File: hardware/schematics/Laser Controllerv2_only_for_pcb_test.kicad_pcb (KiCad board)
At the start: 2 copper layers, 175 x 115 mm, 116 parts, among them J1 SD Card Module (6-pin, 2.54mm), J2 12.6V IN (BUCK), J3 PWR IN Galvo, J4 FAN1 12V IN, J5 FAN1, J6 FAN2 12V IN, J7 FAN2, U1 ESP32-S3-N16R8-DevKit, U10 DS18B20 connector, U12 OPA4134UA_2K5, U13 Galvo Input, U15 6N137, U16 6N137, U17 6N137, U2 DAC8562SDGST, U3 TTL_RGB Blue, U4 TTL_RGB Red, U5 TTL_RGB Green, U6 DS18B20 connector, U7 DS18B20 connector, U8 DS18B20 connector, U9 DS18B20 connector

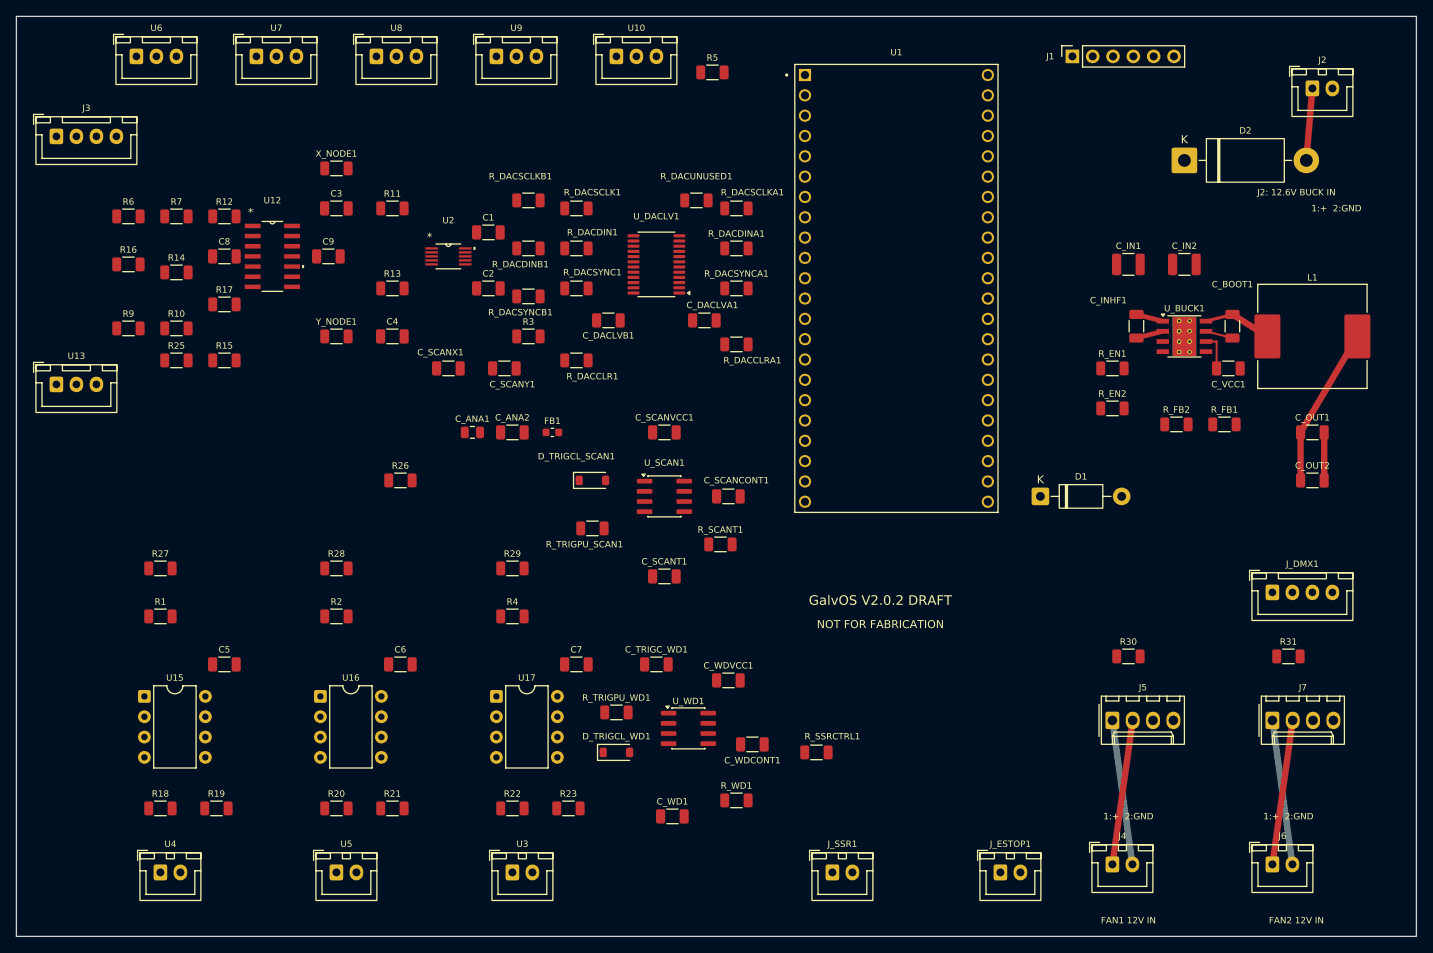
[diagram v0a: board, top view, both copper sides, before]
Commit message: feat(hw): route v2.0.3 draft and add ground planes
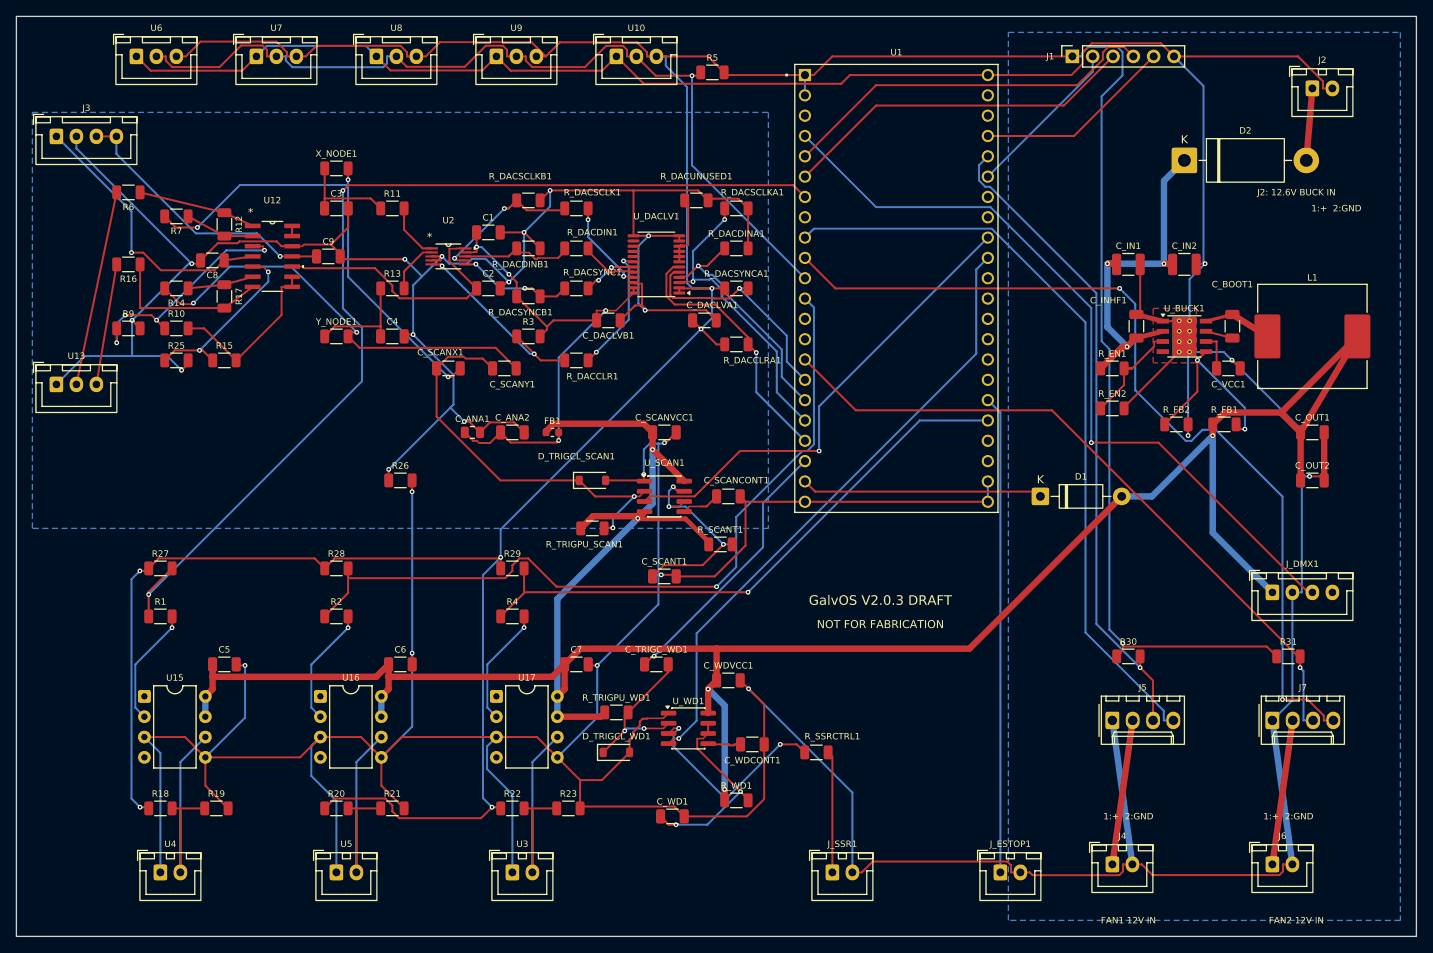
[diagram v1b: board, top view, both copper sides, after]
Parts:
- moved R6 3.00 mm to (14.0, 22.0), turned to 180 degrees
- moved R14 2.00 mm to (20.0, 34.0), turned to 180 degrees
- moved C8 1.58 mm to (24.5, 30.5), turned to 180 degrees
- moved R12 1.00 mm to (26.0, 26.0), turned to -90 degrees
- moved R17 1.00 mm to (26.0, 35.0), turned to -90 degrees
- turned R16 to 180 degrees
- turned R7 to 180 degrees
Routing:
- net 5V GND Buck: track 45.8 -> 788.3 mm, vias 0 -> 12
- net +3V3: track 0.00 -> 456.2 mm, vias 0 -> 7
- net Buck +5V: track 19.9 -> 335.8 mm, vias 0 -> 5
- net AGND (from Galvo Board): track 0.00 -> 249.0 mm, vias 0 -> 13
- net /GPIO7: track 0.00 -> 128.7 mm, vias 0 -> 2
- net /FAN2_PWM: track 0.00 -> 112.7 mm, vias 0 -> 2
- net Net-(U1-GPIO18): track 0.00 -> 111.0 mm, vias 0 -> 1
- net /GPIO8: track 0.00 -> 98.0 mm, vias 0 -> 1
- net /GPIO4: track 0.00 -> 96.9 mm, vias 0 -> 1
- net /FAN1_PWM: track 0.00 -> 95.4 mm
- net /FAN2_TACH: track 0.00 -> 86.6 mm, vias 0 -> 1
- net /FAN1_TACH: track 0.00 -> 81.7 mm, vias 0 -> 1
- net /GPIO38: track 0.00 -> 77.6 mm, vias 0 -> 1
- net /GPIO21: track 0.00 -> 74.1 mm, vias 0 -> 1
- net /+5V_ANA: track 0.00 -> 66.5 mm, vias 0 -> 4
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- added copper zone on B.Cu, net 5V GND Buck
- added copper zone on F.Cu, net 5V GND Buck
- added copper zone on B.Cu, net AGND (from Galvo Board)
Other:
- board text added: "GalvOS V2.0.3 DRAFT"
- board text removed: "GalvOS V2.0.2 DRAFT"

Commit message: fix(hw): buffer scan-status GPIO in v2.0.4
Remove direct 5 V timer drive of GPIO39 while preserving polarity.
Keep the draft unreleased pending safety and physical validation.
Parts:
- added C_SCANLV1: 100nF, Capacitor_SMD:C_1206_3216Metric, F.Cu at (125.5, 31.5)
- added R_SCANIN1: 10k, Resistor_SMD:R_1206_3216Metric, F.Cu at (133.0, 29.0)
- added U_SCANLV1: SN74LVC1G17DBVR, Package_TO_SOT_SMD:SOT-23-5, F.Cu at (128.0, 27.6)
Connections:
- U_SCAN1 pad 3: /GPIO39 -> /SCAN_STATUS_5V
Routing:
- net /SCAN_STATUS_5V: track 0.00 -> 72.8 mm, vias 0 -> 2
- net /GPIO39: track 59.8 -> 5.83 mm, vias 1 -> 0
- net 5V GND Buck: track 788.3 -> 803.7 mm, vias 12 -> 14
- net +3V3: track 456.2 -> 470.9 mm, vias 7 -> 8
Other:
- board text added: "GalvOS V2.0.4 DRAFT"
- board text removed: "GalvOS V2.0.3 DRAFT"

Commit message: fix(hw): protect DMX GPIO in v2.0.5
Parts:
- added C_DMXLV1: 100nF, Capacitor_SMD:C_1206_3216Metric, F.Cu at (125.5, 20.9)
- added R_DMXIN1: 10k, Resistor_SMD:R_1206_3216Metric, F.Cu at (133.0, 18.5)
- added U_DMXLV1: SN74LVC1G17DBVR, Package_TO_SOT_SMD:SOT-23-5, F.Cu at (128.0, 17.0)
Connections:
- J_DMX1 pad 3: /GPIO4 -> /DMX_RO_5V
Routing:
- net /DMX_RO_5V: track 0.00 -> 86.1 mm, vias 0 -> 2
- net /GPIO4: track 96.9 -> 39.0 mm
- net 5V GND Buck: track 803.7 -> 834.0 mm, vias 14 -> 15
- net +3V3: track 470.9 -> 482.8 mm, vias 8 -> 9
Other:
- board text added: "GalvOS V2.0.5 DRAFT"
- board text removed: "GalvOS V2.0.4 DRAFT"

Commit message: fix(hw): shorten buck feedback in v2.0.6
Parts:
- C_INHF1: value 100nF -> 220nF
- moved R_FB2 6.50 mm to (145.2, 44.5), turned to 180 degrees
- moved R_FB1 3.61 mm to (149.0, 48.0), turned to 90 degrees
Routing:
- net /FB_BUCK: track 23.7 -> 6.55 mm, vias 2 -> 0
- net 5V GND Buck: track 834.0 -> 825.4 mm, vias 15 -> 14
- net Buck +5V: track 335.8 -> 337.8 mm
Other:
- board text added: "GalvOS V2.0.6 DRAFT"
- board text removed: "GalvOS V2.0.5 DRAFT"

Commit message: fix(hw): localize buck input loop in v2.0.7
Preserve circuit values while shortening local capacitor paths.
Remove two exact duplicate copper objects and guard ID uniqueness.
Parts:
- moved C_IN2 12.2 mm to (136.5, 38.7), turned to 90 degrees
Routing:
- net +3V3: track 482.8 -> 480.0 mm
- net /VIN_BUCK: track 44.2 -> 46.6 mm, vias 3 -> 2
- net 5V GND Buck: track 825.4 -> 827.8 mm, vias 14 -> 13
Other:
- board text added: "GalvOS V2.0.7 DRAFT"
- board text removed: "GalvOS V2.0.6 DRAFT"
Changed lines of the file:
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@@
 		(title "GalvOS Laser Controller V2")
 		(date "2026-09-14")
-		(rev "V2.0.6 DRAFT")
+		(rev "V2.0.7 DRAFT")
 		(comment 1 "NOT FOR FABRICATION OR LASER OPERATION")
 	)
@@
 	(footprint "Capacitor_SMD:C_1210_3225Metric"
 		(layer "F.Cu")
-		(at 146 31)
+		(at 136.5 38.73 90)
 		(descr "Capacitor SMD 1210 (3225 Metric), square (rectangular) end terminal, IPC-7351 nominal, (Body size source: IPC-SM-782 page 76, https://www.pcb-3d.com/wordpress/wp-content/uploads/ipc-sm-782a_amendment_1_and_2.pdf)")
 		(tags "capacitor")
 		(property "Reference" "C_IN2"
-			(at 0 -2.3 0)
+			(at 4.03 0 0)
 			(layer "F.SilkS")
 			(effects
@@
 		)
 		(property "Value" "10uF"
-			(at 0 2.3 0)
+			(at 0 2.3 90)
 			(layer "F.Fab")
 			(effects
@@
 		)
 		(property "Datasheet" ""
-			(at 0 0 0)
+			(at 0 0 90)
 			(layer "F.Fab")
 			(hide yes)
@@
 		)
 		(property "Description" "Unpolarized capacitor"
-			(at 0 0 0)
+			(at 0 0 90)
 			(layer "F.Fab")
 			(hide yes)
@@
 		)
 		(property "KiLib_Generator" "SMD_2terminal_chip_molded"
-			(at 0 0 0)
+			(at 0 0 90)
 			(layer "F.SilkS")
 			(hide yes)
@@
 		)
 		(fp_text user "${REFERENCE}"
-			(at 0 0 0)
+			(at 0 0 90)
 			(layer "F.Fab")
 			(effects
@@
 		)
 		(pad "1" smd roundrect
-			(at -1.475 0)
+			(at -1.475 0 90)
 			(size 1.15 2.7)
 			(layers "F.Cu" "F.Mask" "F.Paste")
@@
 		)
 		(pad "2" smd roundrect
-			(at 1.475 0)
+			(at 1.475 0 90)
 			(size 1.15 2.7)
 			(layers "F.Cu" "F.Mask" "F.Paste")
@@
 				(font
 					(size 1.27 1.27)
+					(thickness 0.15)
 				)
 			)
@@
 				(font
 					(size 1.27 1.27)
+					(thickness 0.15)
 				)
 			)
@@
 				(font
 					(size 1.27 1.27)
+					(thickness 0.15)
 				)
 			)
@@
 		(tags "capacitor")
 		(property "Reference" "C_INHF1"
-			(at 3.23 -3.5 0)
+			(at 4.23 2.5 0)
 			(layer "F.SilkS")
 			(effects
@@
 				(font
 					(size 1.27 1.27)
+					(thickness 0.15)
 				)
 			)
@@
 				(font
 					(size 1.27 1.27)
+					(thickness 0.15)
 				)
 			)
@@
 				(font
 					(size 1.27 1.27)
+					(thickness 0.15)
 				)
 			)
@@
 		)
 	)
-	(gr_text "GalvOS V2.0.6 DRAFT"
+	(gr_text "GalvOS V2.0.7 DRAFT"
 		(at 108 73 0)
 		(layer "F.SilkS")
@@
 	)
 	(segment
-		(start 85.5913 39.0662)
-		(end 87.5251 41)
-		(width 0.25)
-		(layer "F.Cu")
-		(net "+3V3")
-	)
-	(segment
 		(start 47.8658 100.227)
 		(end 58.087 100.227)
@@
 	)
 	(segment
-		(start 85.5912 39.0662)
-		(end 85.5913 39.0662)
-		(width 0.25)
-		(layer "F.Cu")
-		(net "+3V3")
-	)
-	(segment
 		(start 33.8233 5)
 		(end 33.8233 4.4852)
@@
 	)
 	(segment
-		(start 144.439 30.9138)
-		(end 144.525 31)
-		(width 0.8)
+		(start 135.5375 44)
+		(end 135.538 44)
+		(width 0.25)
 		(layer "F.Cu")
 		(net "/VIN_BUCK")
 	)
 	(segment
-		(start 135.5375 44)
-		(end 135.538 44)
-		(width 0.25)
+		(start 136.5 40.205)
+		(end 140 40.205)
+		(width 0.8)
 		(layer "F.Cu")
 		(net "/VIN_BUCK")
@@
 	)
 	(segment
-		(start 143.447 30.9138)
-		(end 144.439 30.9138)
-		(width 0.8)
-		(layer "F.Cu")
-		(net "/VIN_BUCK")
-	)
-	(segment
 		(start 137.439 30.9138)
 		(end 137.525 31)
@@
 	)
 	(via
-		(at 143.447 30.9138)
-		(size 0.6)
-		(drill 0.3)
-		(layers "F.Cu" "B.Cu")
-		(net "/VIN_BUCK")
-	)
-	(via
 		(at 136.377 30.9138)
 		(size 0.6)
@@
 	)
 	(segment
-		(start 147.561 30.9138)
-		(end 147.475 31)
-		(width 0.25)
-		(layer "F.Cu")
-		(net "5V GND Buck")
-	)
-	(segment
 		(start 23.62 92.62)
 		(end 23.62 96.1575)
@@
 	)
 	(segment
+		(start 136.5 37.255)
+		(end 140 37.255)
+		(width 0.8)
+		(layer "F.Cu")
+		(net "5V GND Buck")
+	)
+	(segment
 		(start 129.138 26.7)
 		(end 129.138 25.8765)
@@
 	)
 	(segment
-		(start 148.59 30.9138)
-		(end 147.561 30.9138)
-		(width 0.25)
-		(layer "F.Cu")
-		(net "5V GND Buck")
-	)
-	(segment
 		(start 46.7569 6.7569)
 		(end 45 5)
@@
 		(size 0.6)
 		(drill 0.3)
-		(layers "F.Cu" "B.Cu")
-		(net "5V GND Buck")
-	)
-	(via
-		(at 148.59 30.9138)
-		(size 0.6)
-		(drill 0.3)

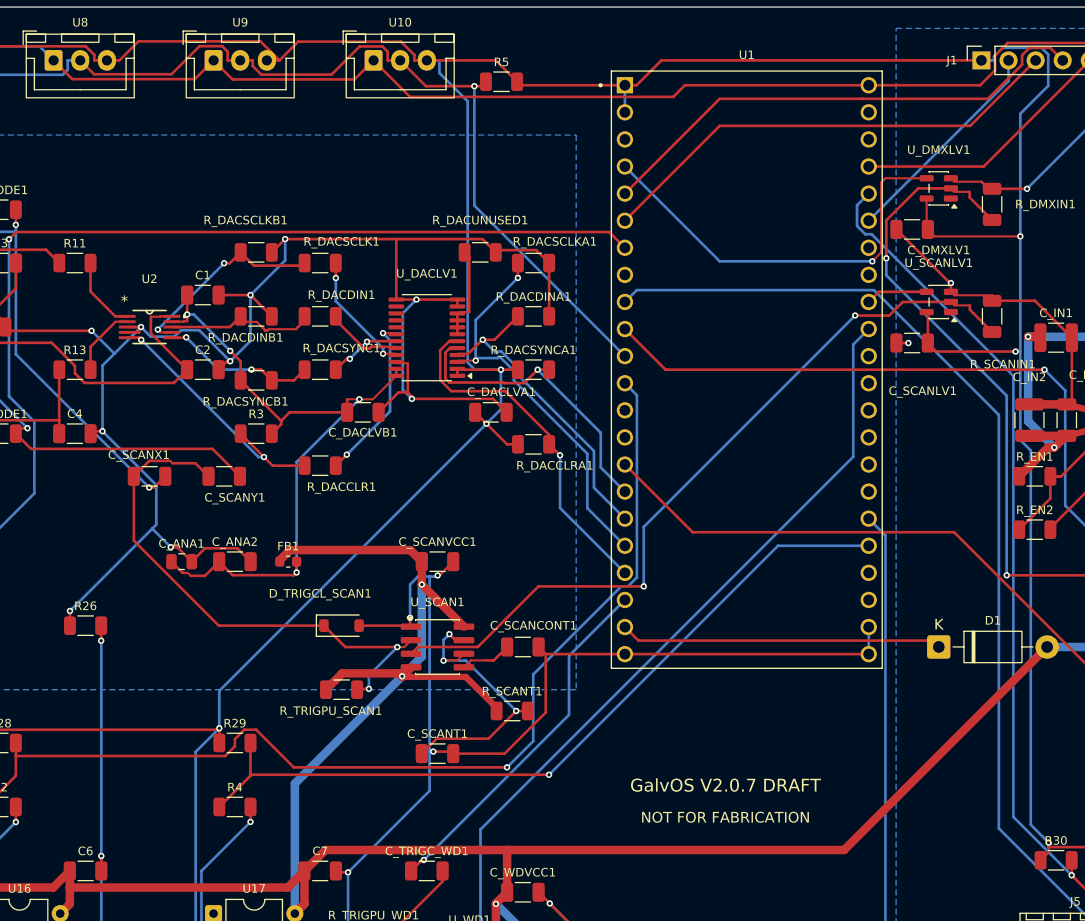
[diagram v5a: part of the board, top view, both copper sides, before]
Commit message: fix(hw): refine return copper and clearance in v2.0.8
Use the reported 28x57 mm module envelope without moving socket pads.
Clear bypass-capacitor collisions and improve local DAC return copper.

Keep the board a draft: row spacing, shutdown, load and physical
qualification remain open. Firmware and KiBot are unchanged.
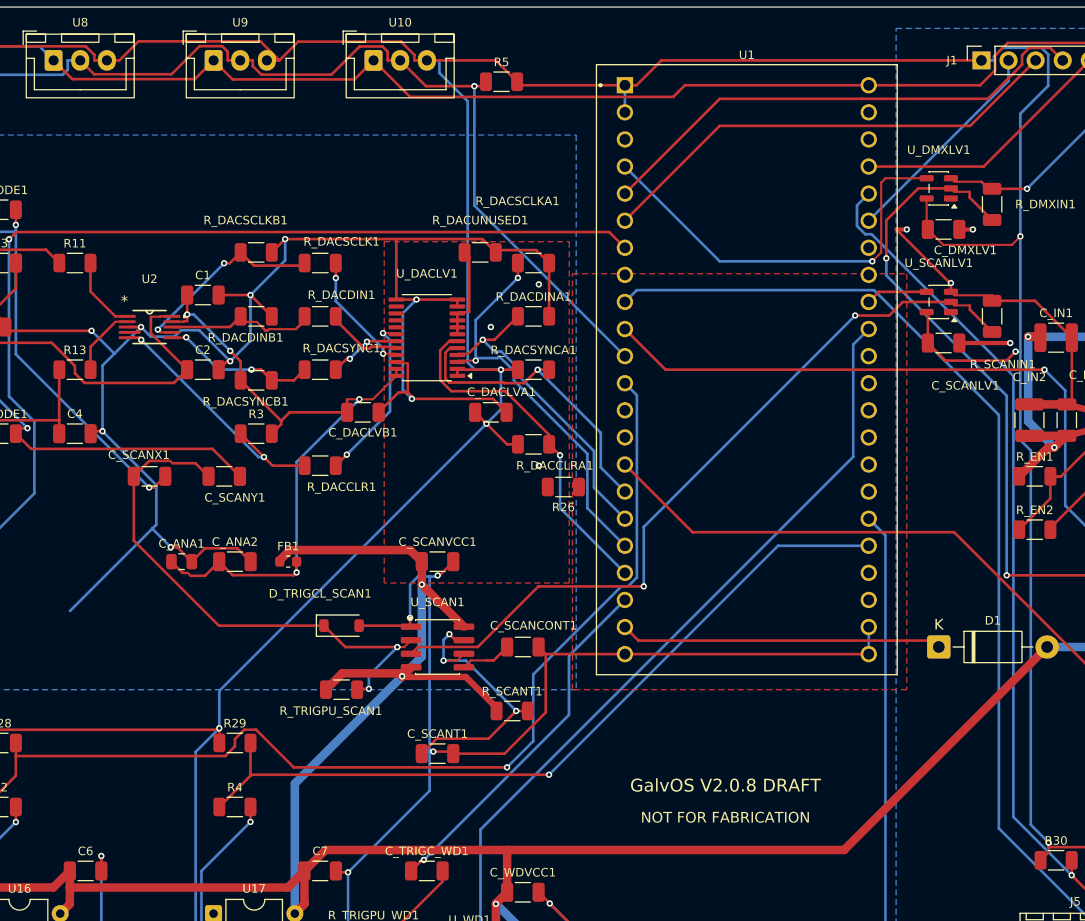
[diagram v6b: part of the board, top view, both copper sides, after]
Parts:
- moved R26 46.6 mm to (92.8, 45.0)
- moved C_DMXLV1 2.95 mm to (128.4, 20.9), turned to 0 degrees
- moved C_SCANLV1 2.95 mm to (128.4, 31.5), turned to 0 degrees
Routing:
- net 5V GND Buck: track 827.8 -> 812.1 mm, vias 13 -> 14
- net AGND (from Galvo Board): track 249.0 -> 247.6 mm, vias 13 -> 15
- net +3V3: track 480.0 -> 481.4 mm
- added copper zone on F.Cu, net AGND (from Galvo Board)
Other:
- board text added: "GalvOS V2.0.8 DRAFT"
- board text removed: "GalvOS V2.0.7 DRAFT"

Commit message: fix(hw): shorten DAC source links in v2.0.9
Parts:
- moved R_DACCLR1 17.3 mm to (73.2, 26.0)
- moved R_DACSCLK1 10.3 mm to (73.2, 33.8)
- moved R_DACSYNC1 6.28 mm to (73.2, 28.6)
- moved R_DACDIN1 3.88 mm to (73.2, 31.2)
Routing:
- net /DAC_CLR_5V: track 24.7 -> 40.5 mm, vias 2 -> 3
- net /DAC_SCLK_5V: track 18.9 -> 31.7 mm
- net Net-(U_DACLV1-B4): track 16.1 -> 6.35 mm, vias 2 -> 0
- net /DAC_SYNC_5V: track 14.5 -> 23.4 mm
- net Net-(U_DACLV1-B1): track 11.6 -> 2.96 mm, vias 2 -> 0
- net Net-(U_DACLV1-B2): track 7.24 -> 2.80 mm
- net /DAC_DIN_5V: track 14.2 -> 17.1 mm
- net Net-(U_DACLV1-B3): track 6.78 -> 4.56 mm, vias 2 -> 0
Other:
- board text added: "GalvOS V2.0.9 DRAFT"
- board text removed: "GalvOS V2.0.8 DRAFT"

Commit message: fix(hw): specify SMD trigger diodes in v2.0.10
Match the existing SOD-123 pads to explicit manufacturer parts and reject recurring package warnings. Copper and connectivity stay unchanged.

Record user exclusion of further thermal, load and timing work; existing limitations remain unverified.
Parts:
- D_TRIGCL_SCAN1, D_TRIGCL_WD1: value 1N4148 -> 1N4148W
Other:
- board text added: "GalvOS V2.0.10 DRAFT"
- board text removed: "GalvOS V2.0.9 DRAFT"
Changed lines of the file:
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@@
 		(title "GalvOS Laser Controller V2")
 		(date "2026-09-14")
-		(rev "V2.0.9 DRAFT")
+		(rev "V2.0.10 DRAFT")
 		(comment 1 "NOT FOR FABRICATION OR LASER OPERATION")
 	)
@@
 			)
 		)
-		(property "Value" "1N4148"
+		(property "Value" "1N4148W"
 			(at 0 2.1 0)
 			(layer "F.Fab")
@@
 			)
 		)
-		(property "Datasheet" "https://assets.nexperia.com/documents/data-sheet/1N4148_1N4448.pdf"
+		(property "Datasheet" "https://www.diodes.com/assets/Datasheets/ds30086.pdf"
 			(at 0 0 0)
 			(unlocked yes)
@@
 			)
 		)
-		(property "Description" "100V 0.15A standard switching diode, DO-35"
+		(property "Description" "100V 300mA fast switching diode, SOD-123; ratings subject to datasheet conditions"
 			(at 0 0 0)
 			(unlocked yes)
@@
 			)
 		)
+		(property "Manufacturer" "Diodes Incorporated"
+			(at 0 0 0)
+			(layer "F.Fab")
+			(hide yes)
+			(effects (font (size 1 1) (thickness 0.15)))
+		)
+		(property "MPN" "1N4148W-7-F"
+			(at 0 0 0)
+			(layer "F.Fab")
+			(hide yes)
+			(effects (font (size 1 1) (thickness 0.15)))
+		)
+		(property "Assembly" "SOD-123; cathode band to pad 1 (trigger); anode pad 2 to power ground. Negative clamp only, not complete timer-input protection."
+			(at 0 0 0)
+			(layer "F.Fab")
+			(hide yes)
+			(effects (font (size 1 1) (thickness 0.15)))
+		)
 		(attr smd)
 		(duplicate_pad_numbers_are_jumpers no)
@@
 			)
 		)
-		(property "Value" "1N4148"
+		(property "Value" "1N4148W"
 			(at 0 2.1 0)
 			(layer "F.Fab")
@@
 			)
 		)
-		(property "Datasheet" "https://assets.nexperia.com/documents/data-sheet/1N4148_1N4448.pdf"
+		(property "Datasheet" "https://www.diodes.com/assets/Datasheets/ds30086.pdf"
 			(at 0 0 0)
 			(unlocked yes)
@@
 			)
 		)
-		(property "Description" "100V 0.15A standard switching diode, DO-35"
+		(property "Description" "100V 300mA fast switching diode, SOD-123; ratings subject to datasheet conditions"
 			(at 0 0 0)
 			(unlocked yes)
@@
 			)
 		)
+		(property "Manufacturer" "Diodes Incorporated"
+			(at 0 0 0)
+			(layer "F.Fab")
+			(hide yes)
+			(effects (font (size 1 1) (thickness 0.15)))
+		)
+		(property "MPN" "1N4148W-7-F"
+			(at 0 0 0)
+			(layer "F.Fab")
+			(hide yes)
+			(effects (font (size 1 1) (thickness 0.15)))
+		)
+		(property "Assembly" "SOD-123; cathode band to pad 1 (trigger); anode pad 2 to power ground. Negative clamp only, not complete timer-input protection."
+			(at 0 0 0)
+			(layer "F.Fab")
+			(hide yes)
+			(effects (font (size 1 1) (thickness 0.15)))
+		)
 		(attr smd)
 		(duplicate_pad_numbers_are_jumpers no)
@@
 		)
 	)
-	(gr_text "GalvOS V2.0.9 DRAFT"
+	(gr_text "GalvOS V2.0.10 DRAFT"
 		(at 108 73 0)
 		(layer "F.SilkS")
